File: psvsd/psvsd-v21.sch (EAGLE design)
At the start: 21 parts, among them U1 GL823(A)OG, U2 3.3V

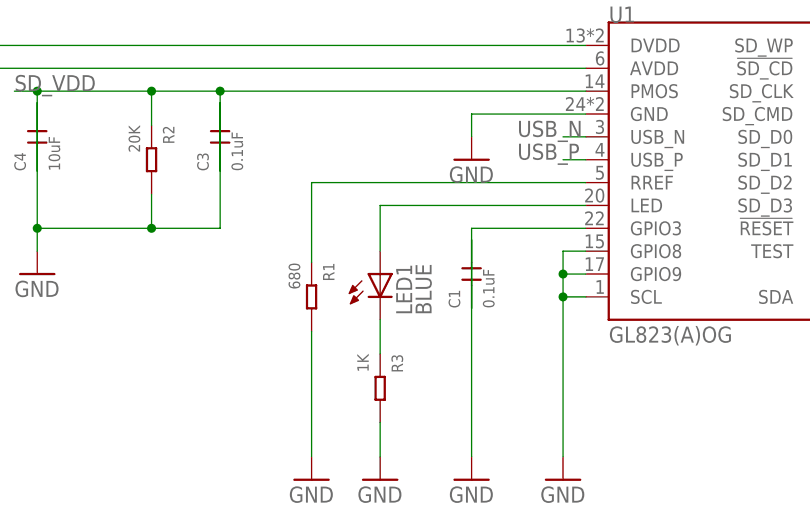
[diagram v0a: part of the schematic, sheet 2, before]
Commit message: Finished silkscreen and added BOM for v2.1 design
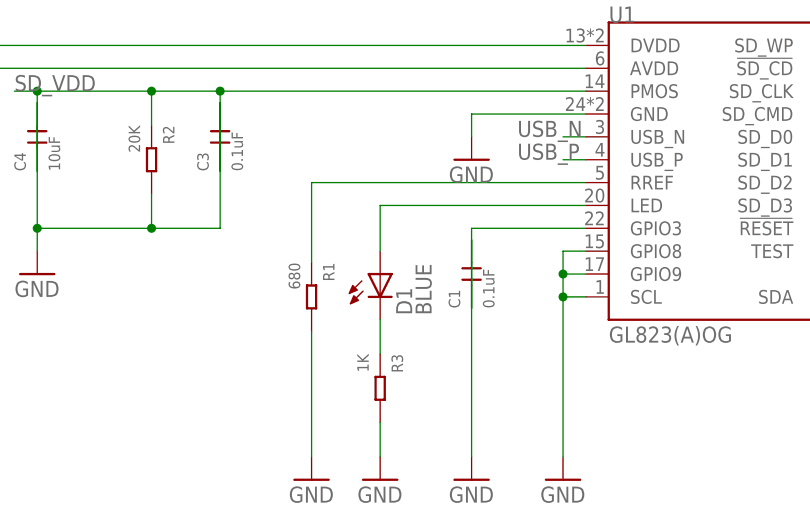
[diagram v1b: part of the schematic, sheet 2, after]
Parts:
- renumbered LED1 to D1
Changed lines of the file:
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@@
 <part name="U2" library="Seeed-IC" library_urn="urn:adsk.eagle:library:470" deviceset="PMIC-LDO-XC6204B332MR(SOT23-5)" device="" value="3.3V"/>
 <part name="R3" library="Seeed-Resistor" library_urn="urn:adsk.eagle:library:474" deviceset="SMD-RES-0R-5%-1/10W(0603)" device="" value="1K"/>
-<part name="LED1" library="led" library_urn="urn:adsk.eagle:library:259" deviceset="LED" device="CHIP-LED0603" value="BLUE"/>
+<part name="D1" library="led" library_urn="urn:adsk.eagle:library:259" deviceset="LED" device="CHIP-LED0603" value="BLUE"/>
 <part name="GND3" library="supply1" library_urn="urn:adsk.eagle:library:371" deviceset="GND" device=""/>
 <part name="GND4" library="supply1" library_urn="urn:adsk.eagle:library:371" deviceset="GND" device=""/>
@@
 <instance part="R2" gate="G$1" x="48.26" y="45.72" rot="R270"/>
 <instance part="R3" gate="G$1" x="73.66" y="20.32" rot="R270"/>
-<instance part="LED1" gate="G$1" x="73.66" y="33.02"/>
+<instance part="D1" gate="G$1" x="73.66" y="33.02"/>
 <instance part="GND3" gate="1" x="66.04" y="10.16"/>
 <instance part="GND4" gate="1" x="35.56" y="33.02"/>
@@
 <wire x1="96.52" y1="40.64" x2="73.66" y2="40.64" width="0.1524" layer="91"/>
 <wire x1="73.66" y1="40.64" x2="73.66" y2="35.56" width="0.1524" layer="91"/>
-<pinref part="LED1" gate="G$1" pin="A"/>
+<pinref part="D1" gate="G$1" pin="A"/>
 </segment>
 </net>
 <net name="LED_N" class="1">
 <segment>
-<pinref part="LED1" gate="G$1" pin="C"/>
+<pinref part="D1" gate="G$1" pin="C"/>
 <wire x1="73.66" y1="27.94" x2="73.66" y2="24.13" width="0.1524" layer="91"/>
 <pinref part="R3" gate="G$1" pin="1"/>

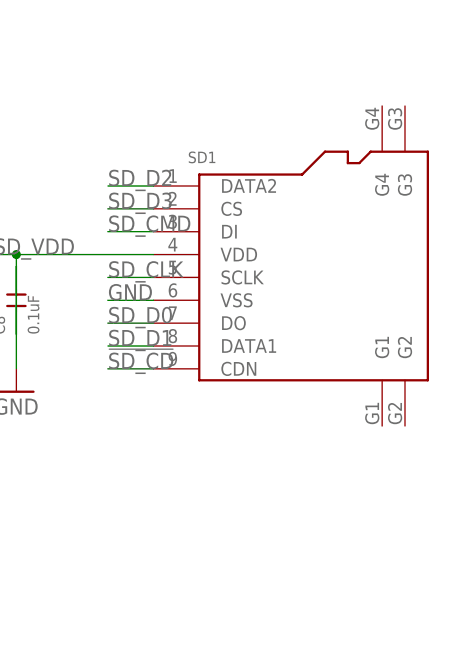
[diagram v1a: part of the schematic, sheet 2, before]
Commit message: Fixed problem where shield is not grounded
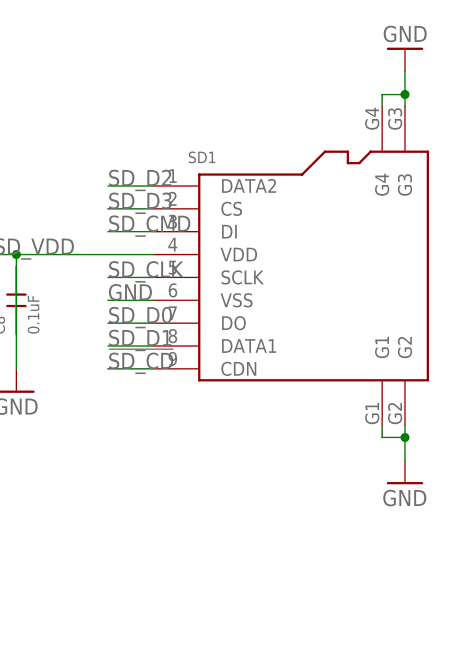
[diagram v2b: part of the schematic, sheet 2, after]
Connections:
- net GND: now also SD1.G1, SD1.G2, SD1.G3, SD1.G4
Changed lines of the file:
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@@
 <part name="JP1" library="pinhead" library_urn="urn:adsk.eagle:library:325" deviceset="PINHD-1X5" device="" value="UART_KERMIT"/>
 <part name="JP2" library="pinhead" library_urn="urn:adsk.eagle:library:325" deviceset="PINHD-1X5" device="" value="UART_SYSCON"/>
+<part name="GND22" library="supply1" library_urn="urn:adsk.eagle:library:371" deviceset="GND" device=""/>
+<part name="GND23" library="supply1" library_urn="urn:adsk.eagle:library:371" deviceset="GND" device=""/>
 </parts>
 <sheets>
@@
 <instance part="GND11" gate="1" x="154.94" y="35.56"/>
 <instance part="GND12" gate="1" x="127" y="63.5" rot="R180"/>
+<instance part="GND22" gate="1" x="198.12" y="73.66" rot="R180"/>
+<instance part="GND23" gate="1" x="198.12" y="25.4"/>
 </instances>
 <busses>
@@
 <pinref part="GND12" gate="1" pin="GND"/>
 </segment>
-</net>
+<segment>
+<pinref part="SD1" gate="G$1" pin="G4"/>
+<wire x1="195.58" y1="67.31" x2="195.58" y2="68.58" width="0.1524" layer="91"/>
+<wire x1="195.58" y1="68.58" x2="198.12" y2="68.58" width="0.1524" layer="91"/>
+<pinref part="SD1" gate="G$1" pin="G3"/>
+<wire x1="198.12" y1="68.58" x2="198.12" y2="67.31" width="0.1524" layer="91"/>
+<wire x1="198.12" y1="68.58" x2="198.12" y2="71.12" width="0.1524" layer="91"/>
+<junction x="198.12" y="68.58"/>
+<pinref part="GND22" gate="1" pin="GND"/>
+</segment>
+<segment>
+<pinref part="SD1" gate="G$1" pin="G1"/>
+<wire x1="195.58" y1="31.75" x2="195.58" y2="30.48" width="0.1524" layer="91"/>
+<pinref part="SD1" gate="G$1" pin="G2"/>
+<wire x1="195.58" y1="30.48" x2="198.12" y2="30.48" width="0.1524" layer="91"/>
+<wire x1="198.12" y1="30.48" x2="198.12" y2="31.75" width="0.1524" layer="91"/>
+<wire x1="198.12" y1="30.48" x2="198.12" y2="27.94" width="0.1524" layer="91"/>
+<junction x="198.12" y="30.48"/>
+<pinref part="GND23" gate="1" pin="GND"/>
+</segment>
+</net>
